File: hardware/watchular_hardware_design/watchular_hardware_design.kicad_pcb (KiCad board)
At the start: 4 copper layers, 55.5 x 22.9 mm, 89 parts, among them J1 USB4105-GF-A, J2 665102131822, J3 TSW-116-07-H-S, J4 TSW-116-07-H-S, Q1 BSS123, Q2 BSS123, Q3 BSS123, Q4 BSS123, T1 DMG1013UW-7, U1 MCP73832T-2DCI/OT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

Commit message: Connected A to B USB pads. No errors or warnings.
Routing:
- net USB_D-: track 40.2 -> 45.1 mm, vias 1 -> 3
- net +5V: track 18.7 -> 15.4 mm
- net USB_D+: track 45.1 -> 47.9 mm
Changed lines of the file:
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@@
         (xy -0.18 0.45)
       ) (layer "B.Paste") (width 0.01) (fill solid))
-    (fp_circle (center -1.238 0.342) (end -1.138 0.342) (layer "B.SilkS") (width 0.2) (fill none))
+    (fp_circle (center 0.254 1.016) (end 0.354 1.016) (layer "B.SilkS") (width 0.2) (fill none))
     (fp_poly (pts
         (xy -0.388581 0.1)
@@
     (fp_line (start -0.5 -0.5) (end 0.5 -0.5) (layer "B.Fab") (width 0.127))
     (fp_line (start 0.5 -0.5) (end 0.5 0.5) (layer "B.Fab") (width 0.127))
-    (fp_circle (center -1.238 0.342) (end -1.138 0.342) (layer "B.Fab") (width 0.2) (fill none))
-    (pad "1" smd custom locked (at -0.45 0.325 180) (size 0.1 0.1) (layers "B.Cu")
+    (fp_circle (center 0.254 1.016) (end 0.354 1.016) (layer "B.Fab") (width 0.2) (fill none))
+    (pad "1" smd custom (at -0.45 0.325 180) (size 0.1 0.1) (layers "B.Cu")
       (net 43 "VDD3P3") (pinfunction "VOUT") (pintype "output") (zone_connect 0)
       (options (clearance outline) (anchor rect))
@@
           ) (width 0.01) (fill yes))
       ))
-    (pad "2" smd custom locked (at -0.45 -0.325 180) (size 0.1 0.1) (layers "B.Cu")
+    (pad "2" smd custom (at -0.45 -0.325 180) (size 0.1 0.1) (layers "B.Cu")
       (net 3 "GND") (pinfunction "GND") (pintype "power_in") (zone_connect 0)
       (options (clearance outline) (anchor rect))
@@
           ) (width 0.01) (fill yes))
       ))
-    (pad "3" smd custom locked (at 0.45 -0.325 180) (size 0.1 0.1) (layers "B.Cu")
+    (pad "3" smd custom (at 0.45 -0.325 180) (size 0.1 0.1) (layers "B.Cu")
       (net 56 "Net-(R7-Pad2)") (pinfunction "EN") (pintype "input") (zone_connect 0)
       (options (clearance outline) (anchor rect))
@@
           ) (width 0.01) (fill yes))
       ))
-    (pad "4" smd custom locked (at 0.45 0.325 180) (size 0.1 0.1) (layers "B.Cu")
+    (pad "4" smd custom (at 0.45 0.325 180) (size 0.1 0.1) (layers "B.Cu")
       (net 55 "VCC") (pinfunction "VIN") (pintype "input") (zone_connect 0)
       (options (clearance outline) (anchor rect))
@@
           ) (width 0.01) (fill yes))
       ))
-    (pad "EP" smd rect locked (at 0 0 135) (size 0.48 0.48) (layers "B.Cu" "B.Paste" "B.Mask")
+    (pad "EP" smd rect (at 0 0 135) (size 0.48 0.48) (layers "B.Cu" "B.Paste" "B.Mask")
       (net 3 "GND") (pinfunction "EXP") (pintype "power_in"))
     (model "/home/borisnotes/projects/Watchular/hardware/kicad-parts/LDO-MIC5524-3-3YMT-TZ/MIC5524-3.3YMT-TZ.step"
@@
   (segment (start 97.399 121.68) (end 98.261501 121.68) (width 0.2) (layer "F.Cu") (net 18))
   (segment (start 100.82 121.705) (end 101.644 120.881) (width 0.2) (layer "F.Cu") (net 18))
+  (segment (start 101.024 120.95) (end 101.644 120.33) (width 0.2) (layer "F.Cu") (net 18))
+  (segment (start 98.52 120.68) (end 98.95 120.25) (width 0.2) (layer "F.Cu") (net 18))
+  (segment (start 97.505 120.68) (end 98.52 120.68) (width 0.2) (layer "F.Cu") (net 18))
+  (segment (start 100.35 120.95) (end 101.024 120.95) (width 0.2) (layer "F.Cu") (net 18))
   (segment (start 98.261501 121.68) (end 98.286501 121.705) (width 0.2) (layer "F.Cu") (net 18))
   (segment (start 101.644 120.11) (end 105.714999 116.039001) (width 0.2) (layer "F.Cu") (net 18))
@@
   (segment (start 123.652798 115.370997) (end 124.807695 116.525894) (width 0.2) (layer "F.Cu") (net 18))
   (segment (start 124.807695 116.525894) (end 124.807695 116.879447) (width 0.2) (layer "F.Cu") (net 18))
+  (via (at 98.95 120.25) (size 0.8) (drill 0.4) (layers "F.Cu" "B.Cu") (net 18))
+  (via (at 100.35 120.95) (size 0.8) (drill 0.4) (layers "F.Cu" "B.Cu") (net 18))
   (via (at 124.807695 116.879447) (size 0.7) (drill 0.3) (layers "F.Cu" "B.Cu") (net 18))
   (segment (start 125.161248 116.879447) (end 124.807695 116.879447) (width 0.2) (layer "B.Cu") (net 18))
@@
   (segment (start 124.807695 116.879447) (end 124.807695 116.525894) (width 0.2) (layer "B.Cu") (net 18))
   (segment (start 125.9405 118.049981) (end 125.9405 117.6587) (width 0.2) (layer "B.Cu") (net 18))
+  (segment (start 99.65 120.25) (end 100.35 120.95) (width 0.2) (layer "B.Cu") (net 18))
   (segment (start 121.854999 113.573198) (end 121.854999 112.314999) (width 0.2) (layer "B.Cu") (net 18))
   (segment (start 124.807695 116.525894) (end 121.854999 113.573198) (width 0.2) (layer "B.Cu") (net 18))
   (segment (start 125.530329 118.460152) (end 125.9405 118.049981) (width 0.2) (layer "B.Cu") (net 18))
   (segment (start 121.854999 112.314999) (end 120.81 111.27) (width 0.2) (layer "B.Cu") (net 18))
+  (segment (start 98.95 120.25) (end 99.65 120.25) (width 0.2) (layer "B.Cu") (net 18))
   (segment (start 111.617851 115.6445) (end 112.285854 114.976497) (width 0.2) (layer "F.Cu") (net 19))
   (segment (start 104.6055 115.6445) (end 111.617851 115.6445) (width 0.2) (layer "F.Cu") (net 19))
@@
   (segment (start 99.07 121.18) (end 104.6055 115.6445) (width 0.2) (layer "F.Cu") (net 19))
   (segment (start 98.286501 122.155) (end 101.269 122.155) (width 0.2) (layer "F.Cu") (net 19))
+  (segment (start 97.505 121.18) (end 96.69 121.18) (width 0.2) (layer "F.Cu") (net 19))
+  (segment (start 96.5 121.37) (end 96.5 121.99) (width 0.2) (layer "F.Cu") (net 19))
+  (segment (start 96.69 121.18) (end 96.5 121.37) (width 0.2) (layer "F.Cu") (net 19))
   (segment (start 124.248249 114.976497) (end 125.479447 116.207695) (width 0.2) (layer "F.Cu") (net 19))
+  (segment (start 96.69 122.18) (end 97.505 122.18) (width 0.2) (layer "F.Cu") (net 19))
+  (segment (start 96.5 121.99) (end 96.69 122.18) (width 0.2) (layer "F.Cu") (net 19))
   (via (at 125.479447 116.207695) (size 0.7) (drill 0.3) (layers "F.Cu" "B.Cu") (net 19))
   (segment (start 125.479447 116.561248) (end 125.479447 116.207695) (width 0.2) (layer "B.Cu") (net 19))
@@
   (segment (start 98.794502 123.844502) (end 98.75 123.8) (width 0.5) (layer "F.Cu") (net 21))
   (segment (start 97.399 123.83) (end 98.72 123.83) (width 0.5) (layer "F.Cu") (net 21))
-  (segment (start 102.05 123.844502) (end 98.794502 123.844502) (width 0.5) (layer "F.Cu") (net 21))
   (segment (start 103.544 123.656) (end 103.5 123.7) (width 0.5) (layer "F.Cu") (net 21))
   (segment (start 103.544 122.53) (end 103.544 123.656) (width 0.5) (layer "F.Cu") (net 21))

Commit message: Added date, company name, place and version.
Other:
- board text added: "2022/07/26 rev V0.1"
- board text added: "Lilordag"
- board text added: "Stockholm, SWE"
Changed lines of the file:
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@@
   (title_block
     (title "Watchular PCB")
-    (date "2022-07-22")
+    (date "2022-07-26")
     (rev "0.1v")
   )
@@
   (gr_line locked (start 92.6 132.86) (end 142.9 132.86) (layer "Edge.Cuts") (width 0.1))
   (gr_line locked (start 90 112.6) (end 90 130.26) (layer "Edge.Cuts") (width 0.1))
+  (gr_text "2022/07/26\nrev V0.1" (at 138.1 114.35 45) (layer "B.SilkS")
+    (effects (font (size 0.918 0.918) (thickness 0.15)) (justify mirror))
+  )
   (gr_text "EN" (at 125.8 130.25) (layer "F.SilkS")
     (effects (font (size 0.918 0.918) (thickness 0.15)))
   )
+  (gr_text "Lilordag" (at 141.55 113.1) (layer "F.SilkS")
+    (effects (font (size 0.918 0.918) (thickness 0.15)))
+  )
   (gr_text "8" (at 107.85 130.2 90) (layer "F.SilkS")
     (effects (font (size 0.918 0.918) (thickness 0.15)))
@@
     (effects (font (size 0.918 0.918) (thickness 0.15)))
   )
-  (gr_text "GND" (at 92.6 127.15) (layer "F.SilkS")
+  (gr_text "GND" (at 94.8 128.05 315) (layer "F.SilkS")
     (effects (font (size 0.918 0.918) (thickness 0.15)))
   )
@@
     (effects (font (size 0.918 0.918) (thickness 0.15)))
   )
-  (gr_text "GND" (at 142.95 127.15) (layer "F.SilkS")
+  (gr_text "GND" (at 140.7 128.05 45) (layer "F.SilkS")
     (effects (font (size 0.918 0.918) (thickness 0.15)))
   )
@@
     (effects (font (size 0.918 0.918) (thickness 0.15)))
   )
+  (gr_text "Stockholm, SWE" (at 144.75 122.1 90) (layer "F.SilkS")
+    (effects (font (size 0.918 0.918) (thickness 0.15)))
+  )
   (gr_text "XP" (at 133.75 113.1 90) (layer "F.SilkS")
     (effects (font (size 0.918 0.918) (thickness 0.15)))
@@
   (segment (start 97.399 119.03) (end 98.88 119.03) (width 0.5) (layer "F.Cu") (net 21))
   (segment (start 98.72 123.83) (end 98.75 123.8) (width 0.5) (layer "F.Cu") (net 21))
-  (segment (start 98.794502 123.844502) (end 98.75 123.8) (width 0.5) (layer "F.Cu") (net 21))
   (segment (start 97.399 123.83) (end 98.72 123.83) (width 0.5) (layer "F.Cu") (net 21))
   (segment (start 103.544 123.656) (end 103.5 123.7) (width 0.5) (layer "F.Cu") (net 21))

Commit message: Added open hardwre logo. Ready for the order.
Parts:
- added REF**: OSHW-Logo2_7.3x6mm_SilkScreen, Symbol:OSHW-Logo2_7.3x6mm_SilkScreen, F.Cu at (93.7, 113.3)

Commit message: Started the BOM.
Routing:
- net VCC: track 9.02 -> 5.14 mm
- net +5V: track 15.3 -> 12.4 mm
- net +BATT: track 25.2 -> 22.8 mm
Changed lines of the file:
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@@
   (segment (start 100.45 117.2875) (end 99 118.7375) (width 0.5) (layer "B.Cu") (net 21))
   (segment (start 102.03 123.824502) (end 102.05 123.844502) (width 0.5) (layer "B.Cu") (net 21))
-  (segment (start 103.5 123.2982) (end 103.8896 122.9086) (width 0.5) (layer "B.Cu") (net 21))
-  (segment (start 102.03 122.55) (end 103.531 122.55) (width 0.5) (layer "B.Cu") (net 21))
   (segment (start 91.3275 120.8775) (end 91.3 120.85) (width 0.3) (layer "B.Cu") (net 21))
-  (segment (start 103.531 122.55) (end 103.8896 122.9086) (width 0.5) (layer "B.Cu") (net 21))
   (segment (start 100.08 123.3525) (end 99.1975 123.3525) (width 0.3) (layer "B.Cu") (net 21))
   (segment (start 99 118.7375) (end 99 119.15) (width 0.5) (layer "B.Cu") (net 21))
   (segment (start 92.45 120.8775) (end 91.3275 120.8775) (width 0.3) (layer "B.Cu") (net 21))
-  (segment (start 103.5 123.7) (end 103.5 123.2982) (width 0.5) (layer "B.Cu") (net 21))
   (segment (start 100.45 116.555) (end 101.155 115.85) (width 0.5) (layer "B.Cu") (net 21))
   (segment (start 99.1975 123.3525) (end 98.75 123.8) (width 0.3) (layer "B.Cu") (net 21))
@@
   (segment (start 94.25 111.25) (end 97.93 111.25) (width 0.5) (layer "B.Cu") (net 45))
   (segment (start 99.33 112.65) (end 97.95 111.27) (width 0.5) (layer "B.Cu") (net 45))
-  (segment (start 105.2104 121.9586) (end 104.1518 120.9) (width 0.5) (layer "B.Cu") (net 45))
   (segment (start 102.35 120.15) (end 102.35 118.9) (width 0.5) (layer "B.Cu") (net 45))
   (segment (start 104.35 116.555) (end 103.645 115.85) (width 0.5) (layer "B.Cu") (net 45))
   (segment (start 102.35 118.9) (end 103.9625 117.2875) (width 0.5) (layer "B.Cu") (net 45))
-  (segment (start 105.2104 122.9086) (end 105.2104 121.9586) (width 0.5) (layer "B.Cu") (net 45))
   (segment (start 103.9625 117.2875) (end 104.35 117.2875) (width 0.5) (layer "B.Cu") (net 45))
   (segment (start 105 115.031604) (end 105 113.3) (width 0.5) (layer "B.Cu") (net 45))
@@
   (segment (start 125.7875 124.16) (end 127.35 122.5975) (width 0.2) (layer "F.Cu") (net 54))
   (segment (start 109.325 122.2) (end 109.503131 122.378131) (width 0.5) (layer "B.Cu") (net 55))
-  (segment (start 104.55 124.9914) (end 105.7611 124.9914) (width 0.5) (layer "B.Cu") (net 55))
-  (segment (start 104.1914 125.35) (end 104.55 124.9914) (width 0.5) (layer "B.Cu") (net 55))
   (segment (start 105.7611 124.9914) (end 107.2525 123.5) (width 0.5) (layer "B.Cu") (net 55))
   (segment (start 107.2525 123.5) (end 107.2525 123.21) (width 0.5) (layer "B.Cu") (net 55))
   (segment (start 107.2525 123.21) (end 108.2625 122.2) (width 0.5) (layer "B.Cu") (net 55))
   (segment (start 108.2625 122.2) (end 109.325 122.2) (width 0.5) (layer "B.Cu") (net 55))
-  (segment (start 102.03 125.35) (end 104.1914 125.35) (width 0.5) (layer "B.Cu") (net 55))
   (segment (start 108.4475 123.5) (end 109.225 123.5) (width 0.3) (layer "B.Cu") (net 56))
   (segment (start 109.225 123.5) (end 109.573842 123.151158) (width 0.3) (layer "B.Cu") (net 56))

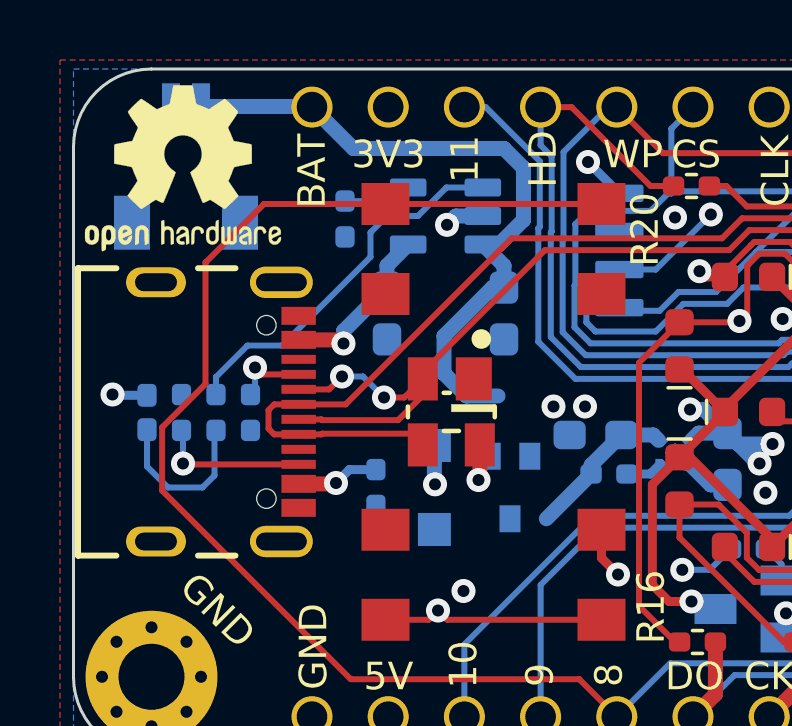
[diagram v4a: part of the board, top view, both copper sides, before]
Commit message: Updated the MOSFTES.
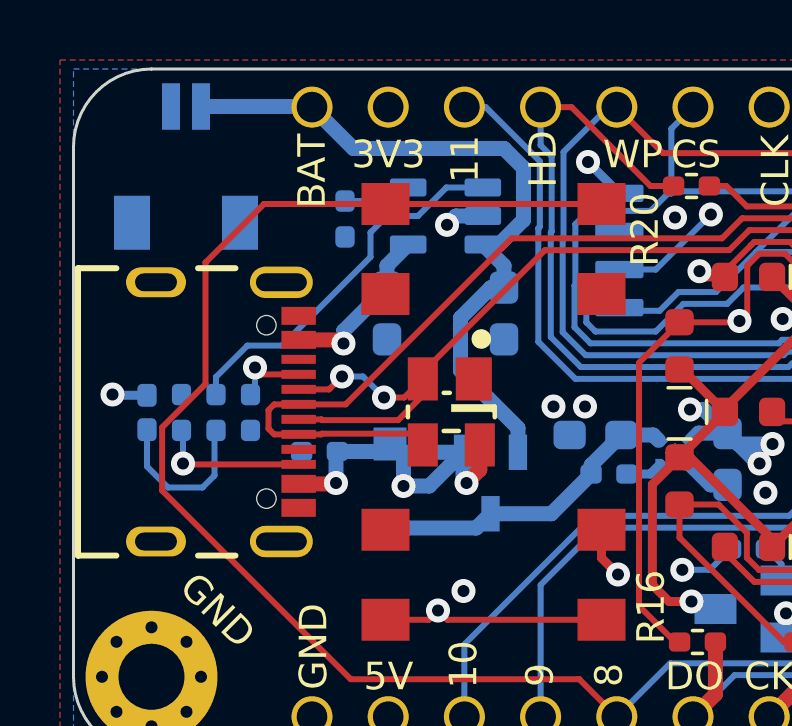
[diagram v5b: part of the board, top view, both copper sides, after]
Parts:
- removed REF**: OSHW-Logo2_7.3x6mm_SilkScreen, Symbol:OSHW-Logo2_7.3x6mm_SilkScreen
- removed T1: DMG1013UW-7, P_MOSFET-DMG1013UW:SOT-323
- added Q5: Q_PMOS_GSD, N_MOSFET_STO91P240X105:SOT91P240X105-3N, B.Cu at (103.9, 123.8)
- moved R6 2.23 mm to (98.2, 122.8), turned to 180 degrees
- moved D1 1.48 mm to (100.5, 123.9)
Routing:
- net +5V: track 12.4 -> 19.6 mm
- net VCC: track 5.14 -> 10.5 mm
- net +BATT: track 22.8 -> 23.9 mm

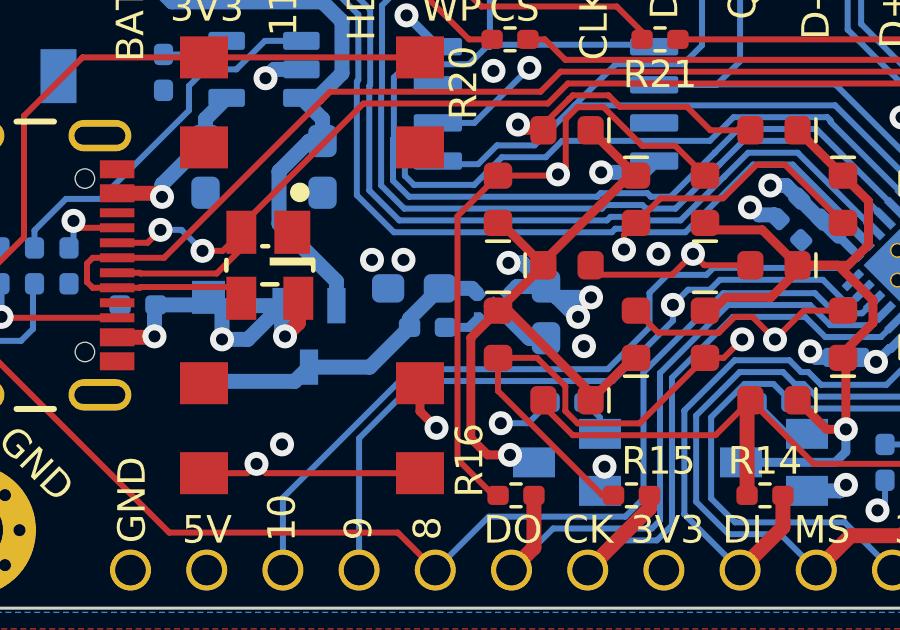
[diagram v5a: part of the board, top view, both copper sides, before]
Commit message: Found suitable LDO (AP7366-33W5-7).
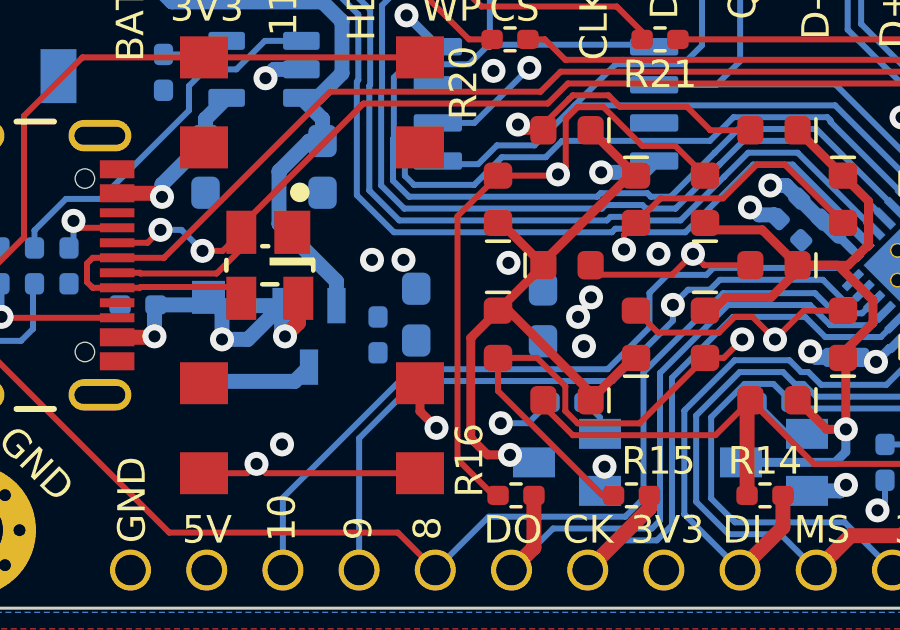
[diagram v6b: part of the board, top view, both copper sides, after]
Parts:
- removed U3: MIC5524-3.3YMT-TZ, LDO-MIC5524-3-3YMT-TZ:VREG_MIC5524-3.3YMT-TZ
- C3, C6: value 2.2uF -> 1uF
- moved R7 1.67 mm to (106.2, 123.8), turned to 90 degrees
- moved C3 0.88 mm to (107.5, 123.1), turned to 90 degrees
- moved C6 0.14 mm to (111.7, 123.1)
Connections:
- R7 pad 2: Net-(R7-Pad2) -> unconnected-(R7-Pad2)
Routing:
- net VCC: track 10.5 -> 3.55 mm
- net VDD3P3: track 23.6 -> 17.7 mm
- net GND: track 26.4 -> 24.5 mm
- net Net-(R7-Pad2): track 1.27 -> 0.00 mm

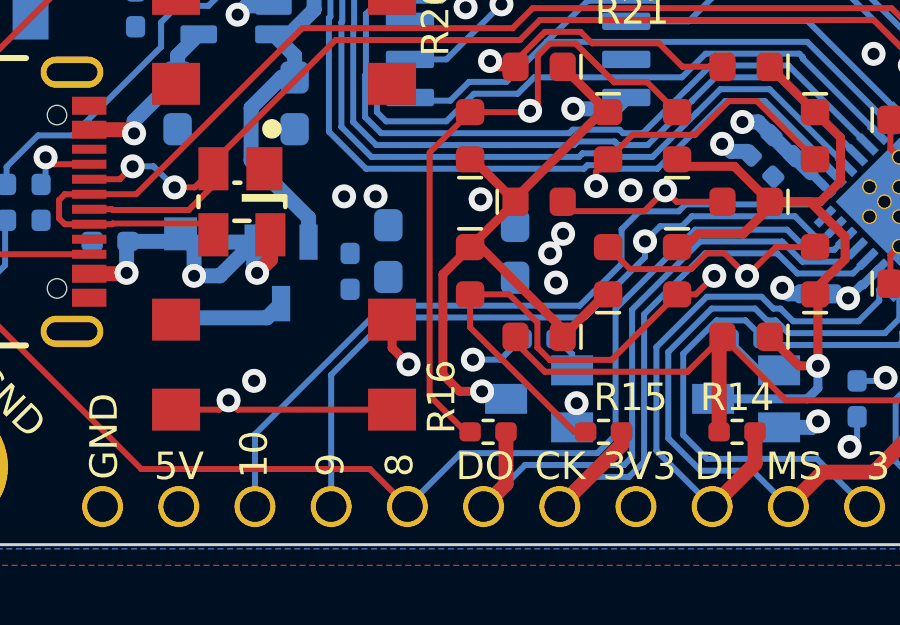
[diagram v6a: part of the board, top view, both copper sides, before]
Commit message: Updated desing with a suitable LDO.
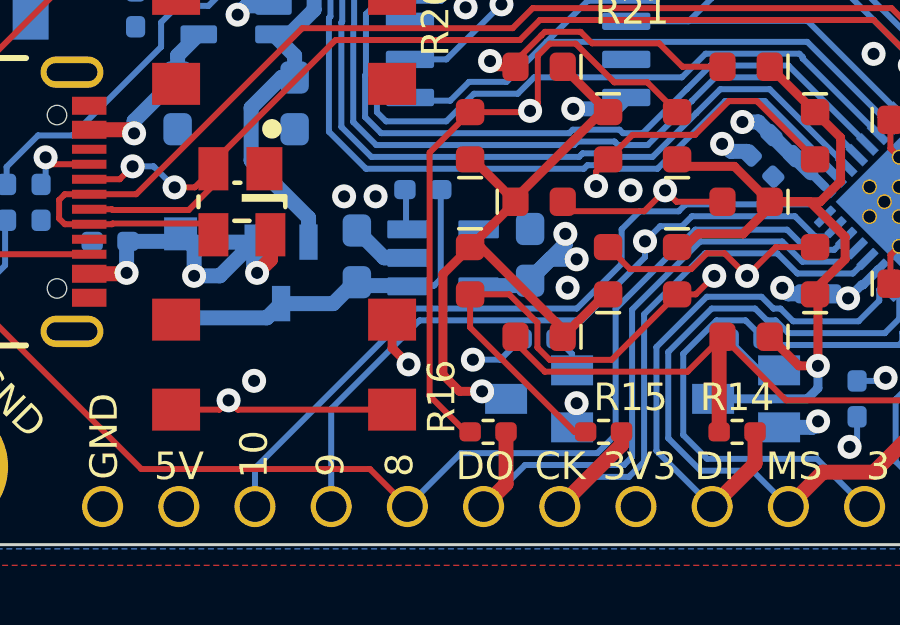
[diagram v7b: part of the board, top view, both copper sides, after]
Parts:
- added VR1: AP7366-33W5-7, LDO-AP7366-33W5-7:SOT95P285X140-5N, B.Cu at (109.3, 123.3)
- moved R7 3.65 mm to (108.6, 121.0), turned to 180 degrees
- moved C3 1.06 mm to (106.4, 123.2)
- moved C6 0.51 mm to (112.2, 123.2), turned to 90 degrees
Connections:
- R7 pad 2: unconnected-(R7-Pad2) -> Net-(R7-Pad2)
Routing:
- net VCC: track 3.55 -> 12.1 mm
- net VDD3P3: track 17.7 -> 23.1 mm, vias 10 -> 9
- net GND: track 24.5 -> 26.5 mm
- net Net-(R7-Pad2): track 0.00 -> 1.26 mm
- net DIGI3_STRAP: track 46.3 -> 45.7 mm
- net DIGI2: track 54.8 -> 54.2 mm
